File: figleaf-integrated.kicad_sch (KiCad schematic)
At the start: 71 parts, among them J1 Conn_01x02_Pin, J2 HRO_TYPE-C-31-M-14, J3 Battery, J9 TC2030_SWD, Q2 2N7002, SW1 PWR, SW2 RST, U1 SRV05-4, U10 MAX17048, U3 BQ24075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

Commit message: update battery conn silkscreen
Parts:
- J1: footprint Connector_PinHeader_1.27mm:PinHeader_1x02_P1.27mm_Vertical -> Graz_Footprints:Generic_Battery_Connector
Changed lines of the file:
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@@
 			)
 		)
-		(property "Footprint" "Connector_PinHeader_1.27mm:PinHeader_1x02_P1.27mm_Vertical"
+		(property "Footprint" "Graz_Footprints:Generic_Battery_Connector"
 			(at 222.25 57.15 0)
 			(effects

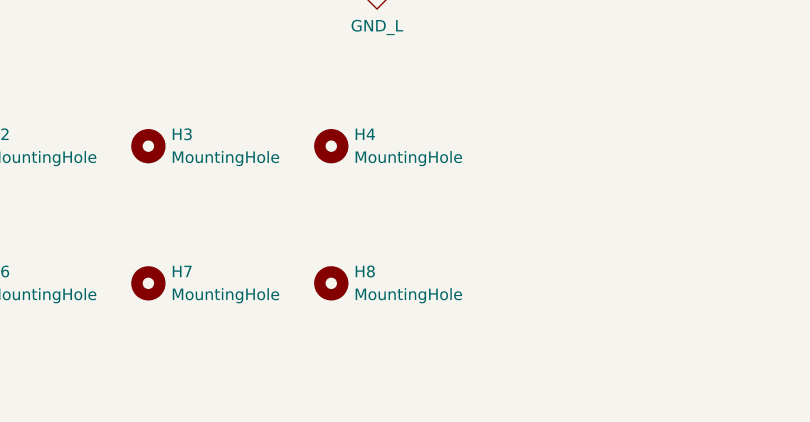
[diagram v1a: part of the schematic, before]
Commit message: reorder & update mt holes count
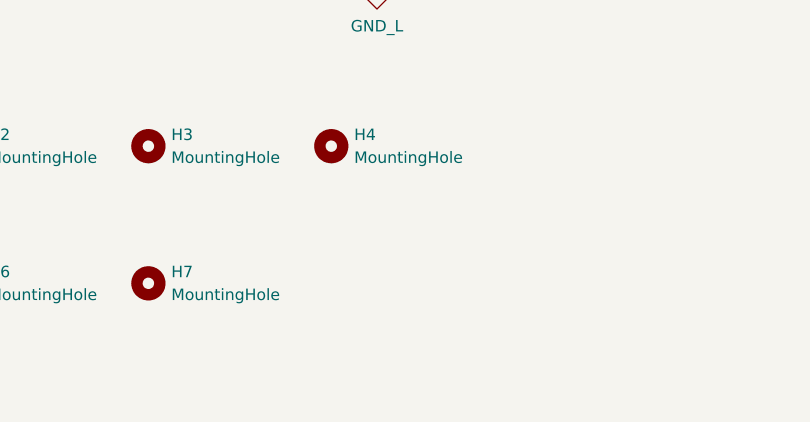
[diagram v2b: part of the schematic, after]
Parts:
- removed H8: MountingHole, Graz_Footprints:m1.6, symbol Mechanical:MountingHole
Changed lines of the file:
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@@
-	)
-	(symbol
-		(lib_id "Mechanical:MountingHole")
-		(at 86.36 226.06 0)
-		(unit 1)
-		(exclude_from_sim no)
-		(in_bom no)
-		(on_board yes)
-		(dnp no)
-		(fields_autoplaced yes)
-		(property "Reference" "H8"
-			(at 88.9 224.7899 0)
-			(effects
-				(font
-					(size 1.27 1.27)
-				)
-				(justify left)
-			)
-		)
-		(property "Value" "MountingHole"
-			(at 88.9 227.3299 0)
-			(effects
-				(font
-					(size 1.27 1.27)
-				)
-				(justify left)
-			)
-		)
-		(property "Footprint" "Graz_Footprints:m1.6"
-			(at 86.36 226.06 0)
-			(effects
-				(font
-					(size 1.27 1.27)
-				)
-				(hide yes)
-			)
-		)
-		(property "Datasheet" "~"
-			(at 86.36 226.06 0)
-			(effects
-				(font
-					(size 1.27 1.27)
-				)
-				(hide yes)
-			)
-		)
-		(property "Description" "Mounting Hole without connection"
-			(at 86.36 226.06 0)
-			(effects
-				(font
-					(size 1.27 1.27)
-				)
-				(hide yes)
-			)
-		)
-		(instances
-			(project "figleaf-integrated"
-				(path "/49b93484-acc8-4f70-93bc-7a6072a35fe8"
-					(reference "H8")
-					(unit 1)
-				)
-			)
-		)
 	)
 	(symbol

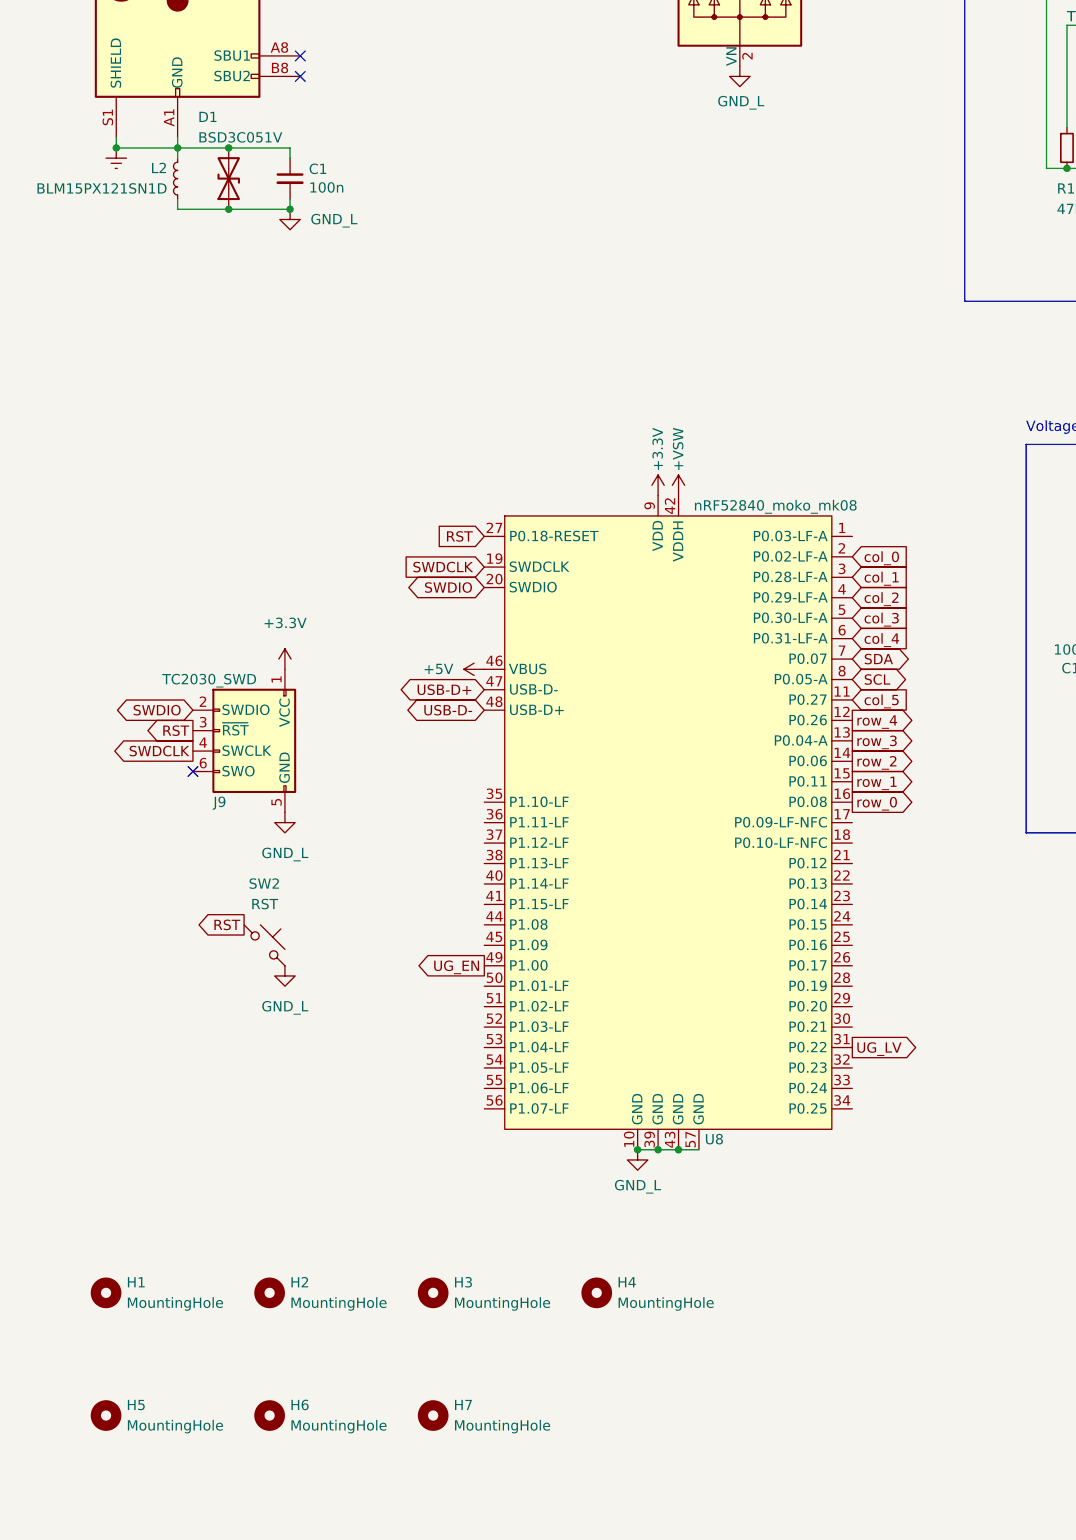
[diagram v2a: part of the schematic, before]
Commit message: move batt conn
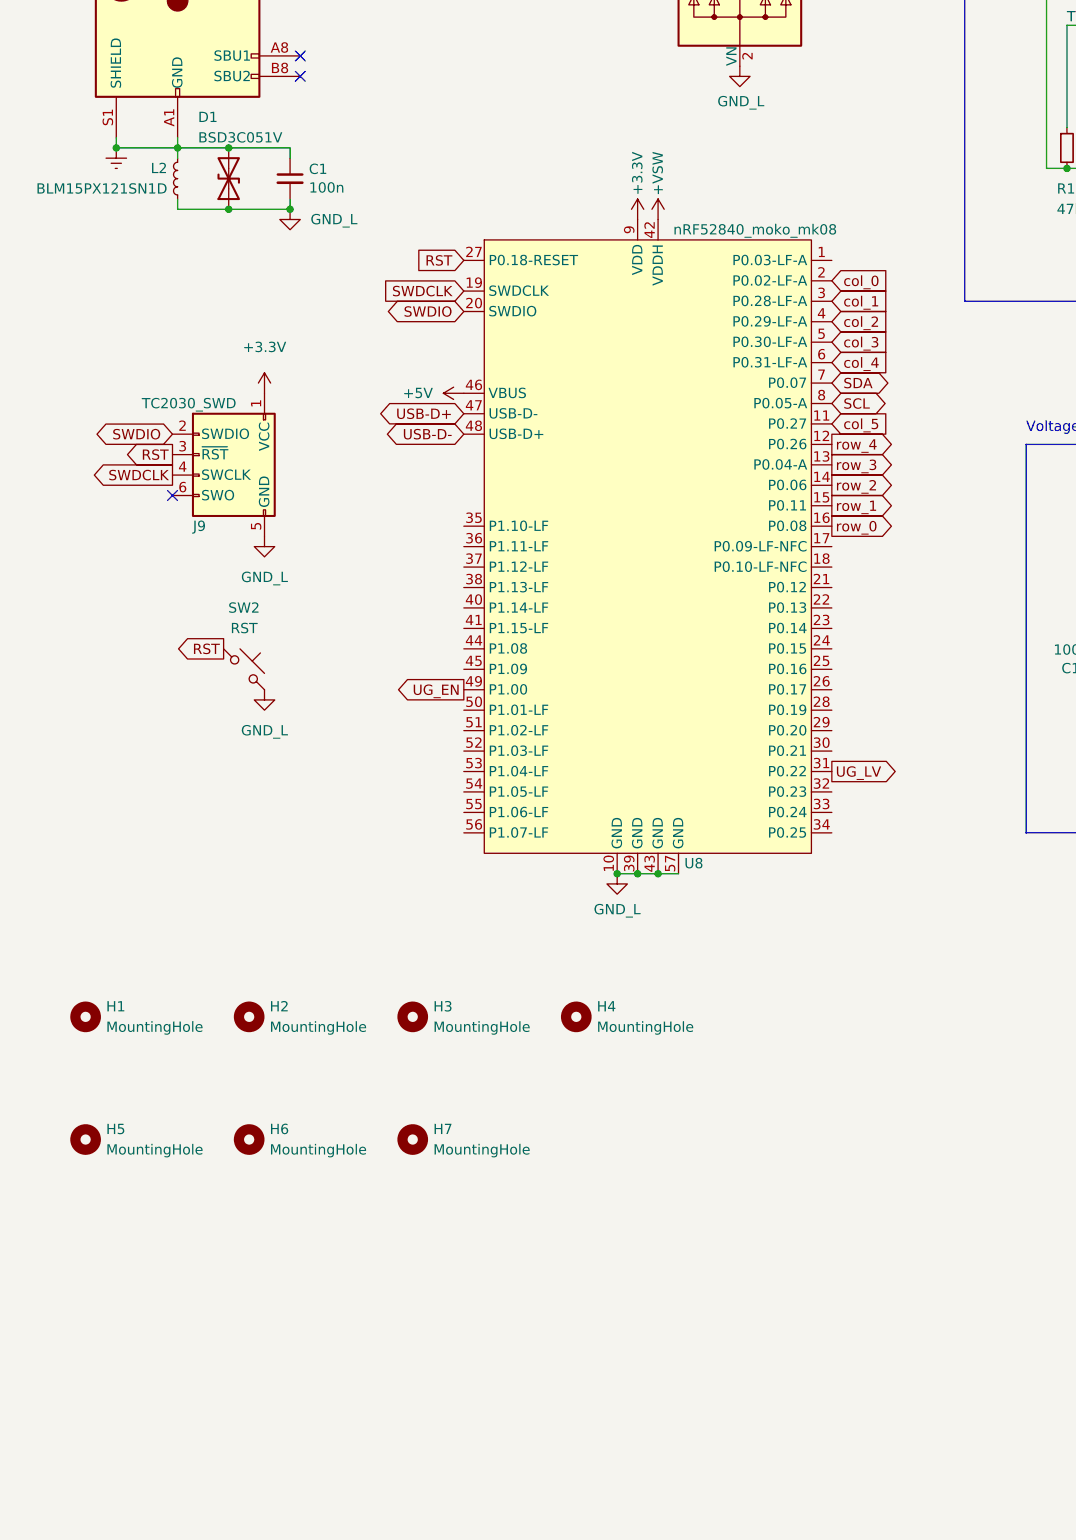
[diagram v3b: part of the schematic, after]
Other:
- moved on the sheet: H1, H2, H3, H4, H5, H6, H7, J9, SW2, U8

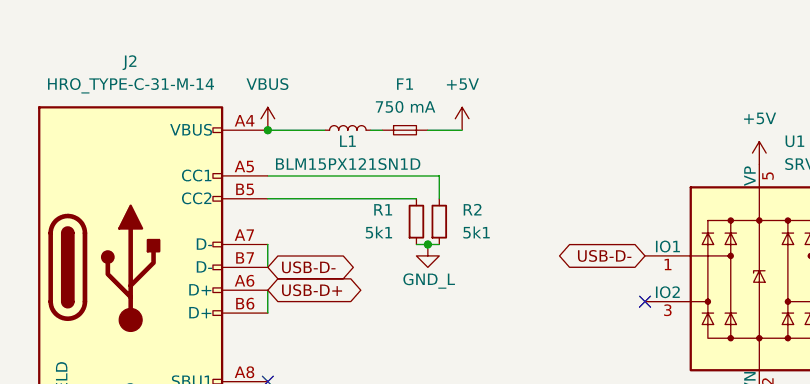
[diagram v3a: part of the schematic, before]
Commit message: update to polyfuse & move silkscreens
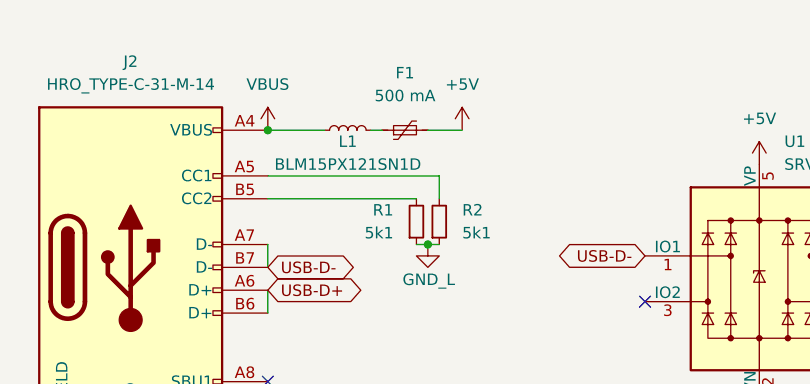
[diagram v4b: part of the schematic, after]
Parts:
- F1: value 750 mA -> 500 mA; footprint Fuse:Fuse_0603_1608Metric -> Fuse:Fuse_1206_3216Metric; symbol Device:Fuse_Small -> Device:Polyfuse_Small
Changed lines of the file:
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@@
 	)
 	(symbol
-		(lib_id "Device:Fuse_Small")
-		(at 64.77 29.21 0)
+		(lib_id "Device:Polyfuse_Small")
+		(at 64.77 29.21 90)
 		(unit 1)
 		(exclude_from_sim no)
@@
 		(fields_autoplaced yes)
 		(property "Reference" "F1"
-			(at 64.77 24.13 0)
+			(at 64.77 22.86 90)
 			(effects
 				(font
@@
 			)
 		)
-		(property "Value" "750 mA"
-			(at 64.77 26.67 0)
+		(property "Value" "500 mA"
+			(at 64.77 25.4 90)
 			(effects
 				(font
@@
 			)
 		)
-		(property "Footprint" "Fuse:Fuse_0603_1608Metric"
-			(at 64.77 29.21 0)
+		(property "Footprint" "Fuse:Fuse_1206_3216Metric"
+			(at 69.85 27.94 0)
 			(effects
 				(font
 					(size 1.27 1.27)
 				)
+				(justify left)
 				(hide yes)
 			)
@@
 			)
 		)
-		(property "Description" "Fuse, small symbol"
+		(property "Description" "Resettable fuse, polymeric positive temperature coefficient, small symbol"
 			(at 64.77 29.21 0)
 			(effects

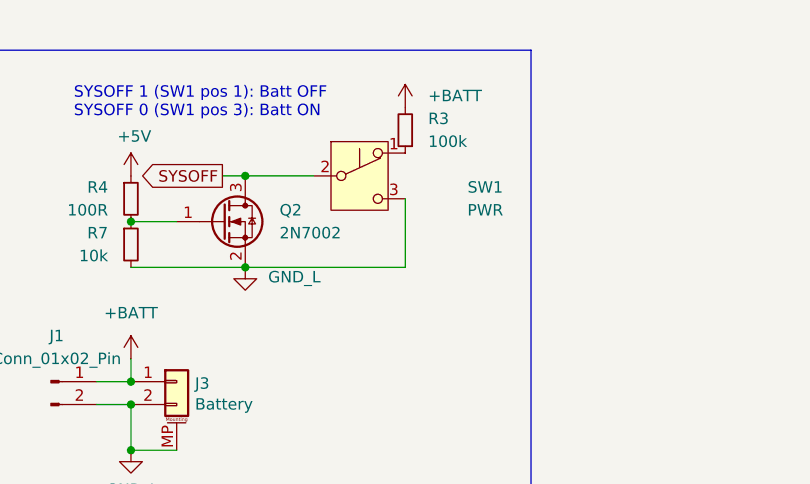
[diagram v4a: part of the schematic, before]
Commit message: Add alps pwr sw
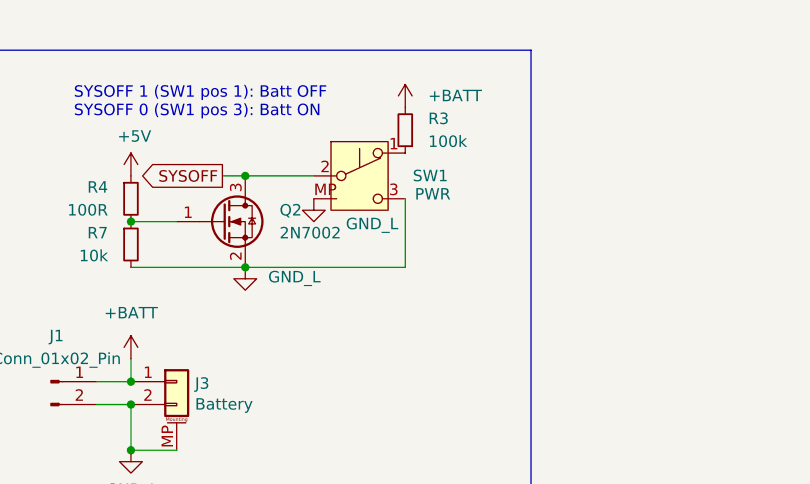
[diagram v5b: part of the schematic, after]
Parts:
- SW1: footprint PCM_marbastlib-various:SW_MSK12C02-HB -> Graz_Footprints:SW_SSSS811101
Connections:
- net GND_L: now also SW1.MP
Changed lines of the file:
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@@
+	)
+	(symbol
+		(lib_id "power:GND")
+		(at 251.46 36.83 0)
+		(unit 1)
+		(exclude_from_sim no)
+		(in_bom yes)
+		(on_board yes)
+		(dnp no)
+		(property "Reference" "#PWR03"
+			(at 251.46 43.18 0)
+			(effects
+				(font
+					(size 1.27 1.27)
+				)
+				(hide yes)
+			)
+		)
+		(property "Value" "GND_L"
+			(at 255.016 39.624 0)
+			(effects
+				(font
+					(size 1.27 1.27)
+				)
+				(justify left)
+			)
+		)
+		(property "Footprint" ""
+			(at 251.46 36.83 0)
+			(effects
+				(font
+					(size 1.27 1.27)
+				)
+				(hide yes)
+			)
+		)
+		(property "Datasheet" ""
+			(at 251.46 36.83 0)
+			(effects
+				(font
+					(size 1.27 1.27)
+				)
+				(hide yes)
+			)
+		)
+		(property "Description" "Power symbol creates a global label with name \"GND\" , ground"
+			(at 251.46 36.83 0)
+			(effects
+				(font
+					(size 1.27 1.27)
+				)
+				(hide yes)
+			)
+		)
+		(pin "1"
+		)
+		(instances
+			(project "figleaf-integrated"
+				(path "/49b93484-acc8-4f70-93bc-7a6072a35fe8"
+					(reference "#PWR03")
+					(unit 1)
+				)
+			)
+		)
 	)
 	(symbol
@@
 		(dnp no)
 		(property "Reference" "SW1"
-			(at 270.51 35.56 0)
+			(at 264.414 34.29 0)
 			(effects
 				(font
@@
 		)
 		(property "Value" "PWR"
-			(at 270.51 38.1 0)
-			(effects
-				(font
-					(size 1.27 1.27)
-				)
-			)
-		)
-		(property "Footprint" "PCM_marbastlib-various:SW_MSK12C02-HB"
-			(at 256.54 34.29 0)
+			(at 264.668 36.322 0)
+			(effects
+				(font
+					(size 1.27 1.27)
+				)
+			)
+		)
+		(property "Footprint" "Graz_Footprints:SW_SSSS811101"
+			(at 257.81 39.878 0)
 			(effects
 				(font
@@
 		)
 		(property "Description" "Momentary Switch, single pole double throw"
-			(at 256.54 34.29 0)
+			(at 257.556 28.194 0)
 			(effects
 				(font
@@
 		(pin "3"
 		)
-		(instances
+		(pin "MP"
+		)
+		(instances
